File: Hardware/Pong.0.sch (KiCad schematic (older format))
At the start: 42 parts, among them IC1 ATMEGA644P-A, J1 DC, J2 USBMICRO-B, P1 ISP, SW1 SPST, X1 20 MHz

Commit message: Fleshed out main project, corrected errors, updated Project Log
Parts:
- removed BT1: 7.2VDC, symbol BATTERY
- removed C1, C10, C11, C2, C6, C7, C8: .1uF, symbol CSMALL
- removed C3, C9: 10uF, symbol CSMALL
- removed C4, C5: 8pF, symbol CSMALL
- removed IC1: ATMEGA644P-A, TQFP44, symbol ATMEGA644P-A
- removed J1: DC, symbol CONN_2
- removed J2: USBMICRO-B, symbol USBMICRO-B
- removed L1: 33uH, symbol INDUCTOR
- removed P1: ISP, symbol CONN_3X2
- removed R1, R2: 10k, symbol R
- removed R10, R11, R12, R13, R14, R15, R16, R17, R18, R19, R20, R21, R22, R3, R4, R5, R6, R7, R8, R9: 10K, symbol R
- removed S1: TL3315NF160Q, symbol TL3315NF160Q
- removed SW1: SPST, symbol SPST
- removed X1: 20 MHz, symbol CRYSTAL
- added BT?: BATTERY, symbol BATTERY
- added C? (x7): .1uF, symbol CSMALL
- added C? (x2): 8pF, symbol CSMALL
- added C? (x2): 10uF, symbol CSMALL
- added IC?: ATMEGA644P-A, TQFP44, symbol ATMEGA644P-A
- added L?: 33uH, symbol INDUCTOR
- added P?: CONN_2, symbol CONN_2
- added P?: ISP, symbol CONN_3X2
- added R?: R, symbol R
- added S?: TL3315NF160Q, symbol TL3315NF160Q
- added U?: USBMICRO-B, symbol USBMICRO-B
- added U?: SPX29150T-L-5-0/TR, symbol SPX29150T-L-5-0/TR
- added X?: 20MHz, symbol CRYSTAL
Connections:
- net labels added: X4, X5, X6, YA0, YA1, YA2, YB0, YB1, YB2
- net labels removed: +5V, SPX29150T-L-5-0/TR, SlaveSelect, UU00, UU01, UU02, UU03, UU04, UU05, UU06, UU07, UU08, UU09, UU10, UU11, UU12, UU13, UU14, UU15, UU16, UU17, UU18, UU19, Y0A, Y0B
- wire segments 158 -> 91

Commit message: Updated BOM and Requirements Document
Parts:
- removed BT?: BATTERY, symbol BATTERY
- removed C? (x7): .1uF, symbol CSMALL
- removed C? (x2): 8pF, symbol CSMALL
- removed C? (x2): 10uF, symbol CSMALL
- removed IC?: ATMEGA644P-A, TQFP44, symbol ATMEGA644P-A
- removed L?: 33uH, symbol INDUCTOR
- removed P?: CONN_2, symbol CONN_2
- removed P?: ISP, symbol CONN_3X2
- removed R?: R, symbol R
- removed S?: TL3315NF160Q, symbol TL3315NF160Q
- removed U?: USBMICRO-B, symbol USBMICRO-B
- removed U?: SPX29150T-L-5-0/TR, symbol SPX29150T-L-5-0/TR
- removed X?: 20MHz, symbol CRYSTAL
- added IC?: ATXMEGA64A4U-A, TQFP44, symbol ATXMEGA64A4U-A
- added U?: TPS61240, symbol TPS61240
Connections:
- net labels removed: AIN0, GND, MISO, MOSI, RESET, SCK, SMP, VCC, X0, X1, X2, X3, X4, X5, X6, YA0, YA1, YA2, YB0, YB1, YB2
- wire segments 91 -> 0
- no-connect marks 3 -> 0
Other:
- note added: "5V 0.45A\nBoost\nRegulator"
- note removed: "+"
- note removed: "-"

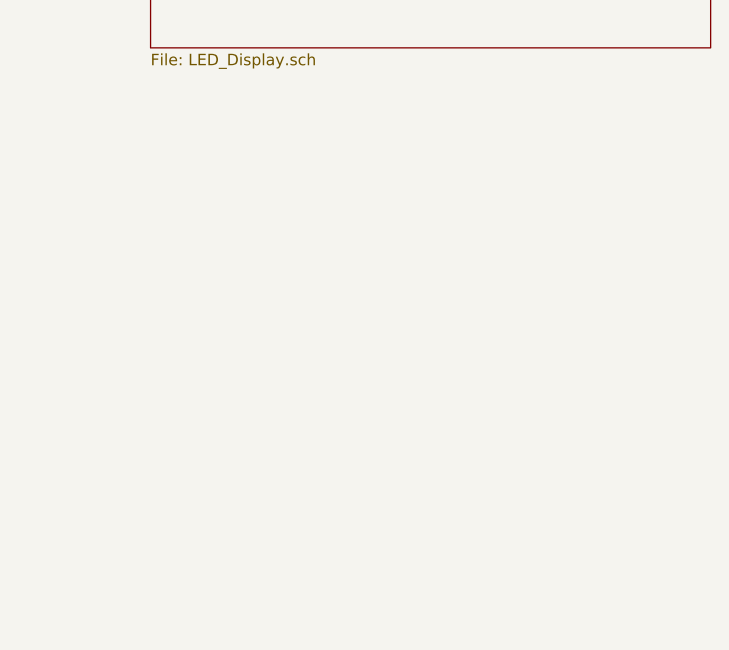
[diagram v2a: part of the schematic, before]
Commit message: Updated BOM and Schematic with significant components
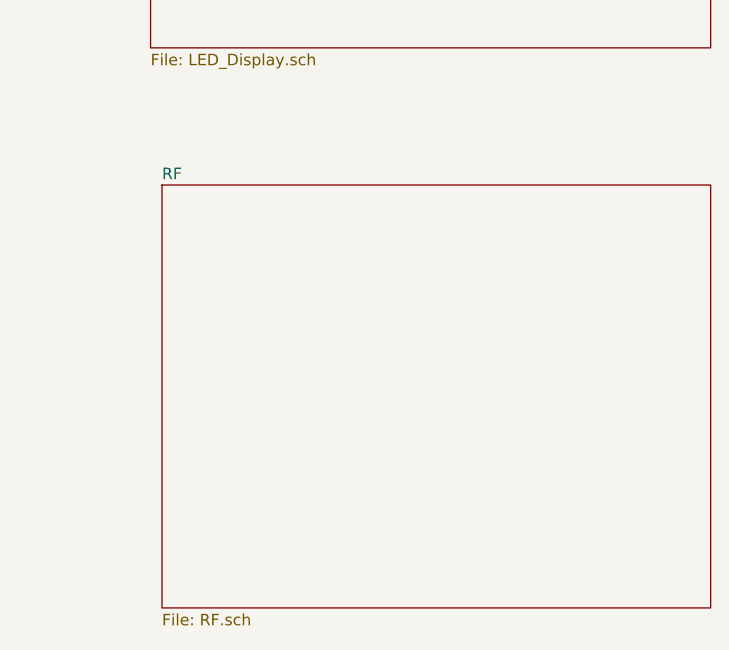
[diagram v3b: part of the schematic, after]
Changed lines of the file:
@@
 $Descr B 17000 11000
 encoding utf-8
-Sheet 1 2
+Sheet 1 3
 Title "Pong.0"
 Date "6 sep 2013"
@@
 6E 56 52 49 51 4E 59 71 7E 65 C5 4D 0F AF 00 BF F6 21 9D BA 45 88 9C 00 16 00 C0 66 90 E0 00 00
 AC 42 3B 38 00 00 AB 90 E0 00 00 AC 42 82 03 00 B0 EA FF 00 E3 76 B5 A7 81 B6 BC 08 00 00 00 00
-49 45 4E 44 AE 42 60 82 36 $EndBitmap
+49 45 4E 44 AE 42 60 82 7D $EndBitmap
 EndData
 $EndBitmap
@@
 Text Notes 6100 2100 0    60   ~ 0
 5V 0.45A\nBoost\nRegulator
+$Sheet
+S 13650 5150 2400 1850
+U 522A0B3B
+F0 "RF" 50
+F1 "RF.sch" 50
+$EndSheet
 $EndSCHEMATC

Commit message: Updated Schematic with Battery Manager and updated some uC pins
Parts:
- removed U?: TPS61240, symbol TPS61240
- added C? (x4): 0.1uF, ~, symbol CSMALL
- added C? (x2): 10uF, ~, symbol CSMALL
- added L?: 10uH, ~, symbol INDUCTOR
- added L?: BEAD, ~, symbol INDUCTOR
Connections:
- net labels added: 3_3V, GND, SCL, SDA, X0, X1, X2, X3, X4, X5, X6, X7, Y0A, Y0B, Y1A, Y1B, Y2A, Y2B, Y3A, Y3B
- wire segments 0 -> 45
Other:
- note removed: "5V 0.45A\nBoost\nRegulator"

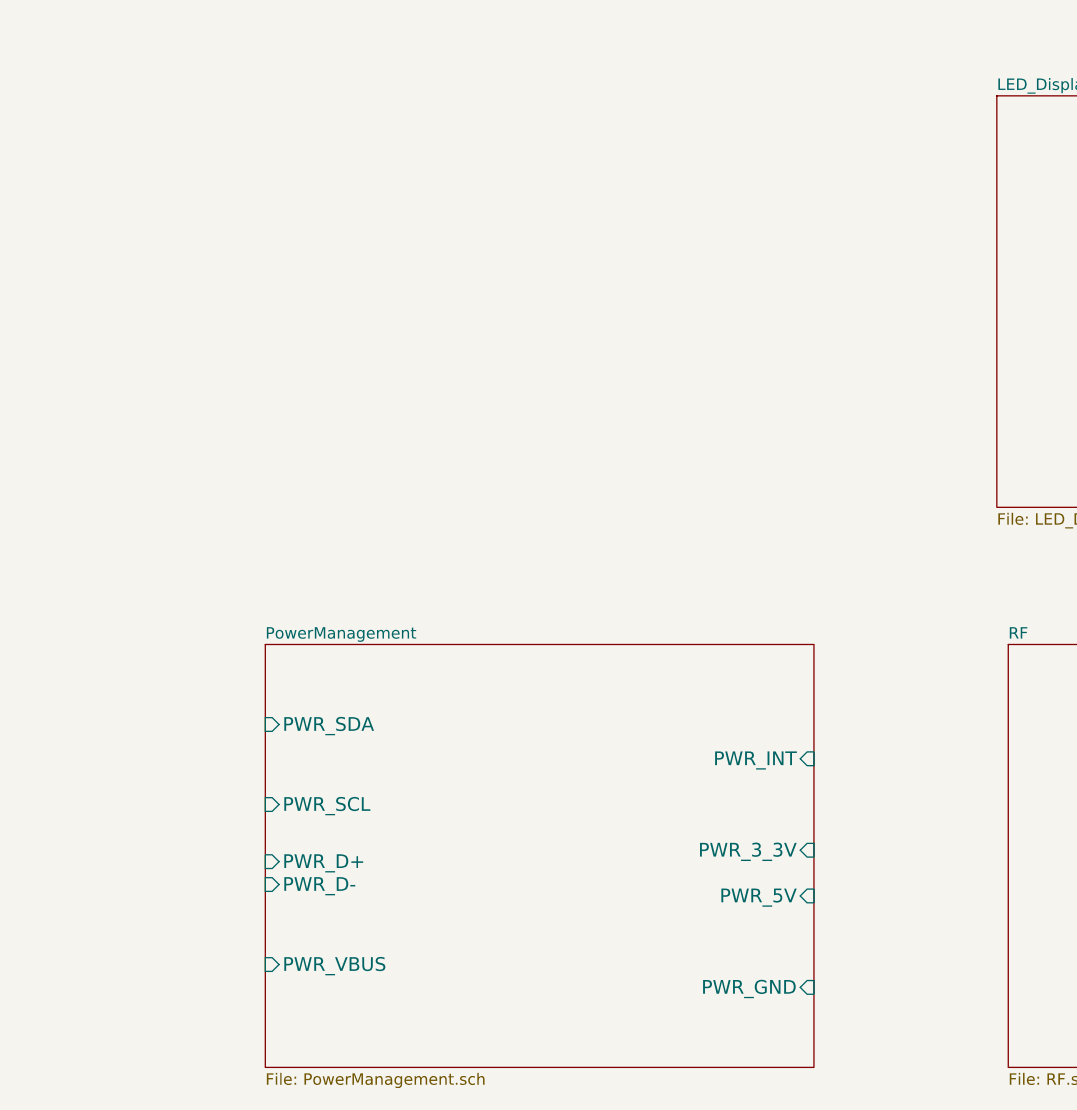
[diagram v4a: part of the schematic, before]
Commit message: Added sheet for QMatrix Sensors and Sliders
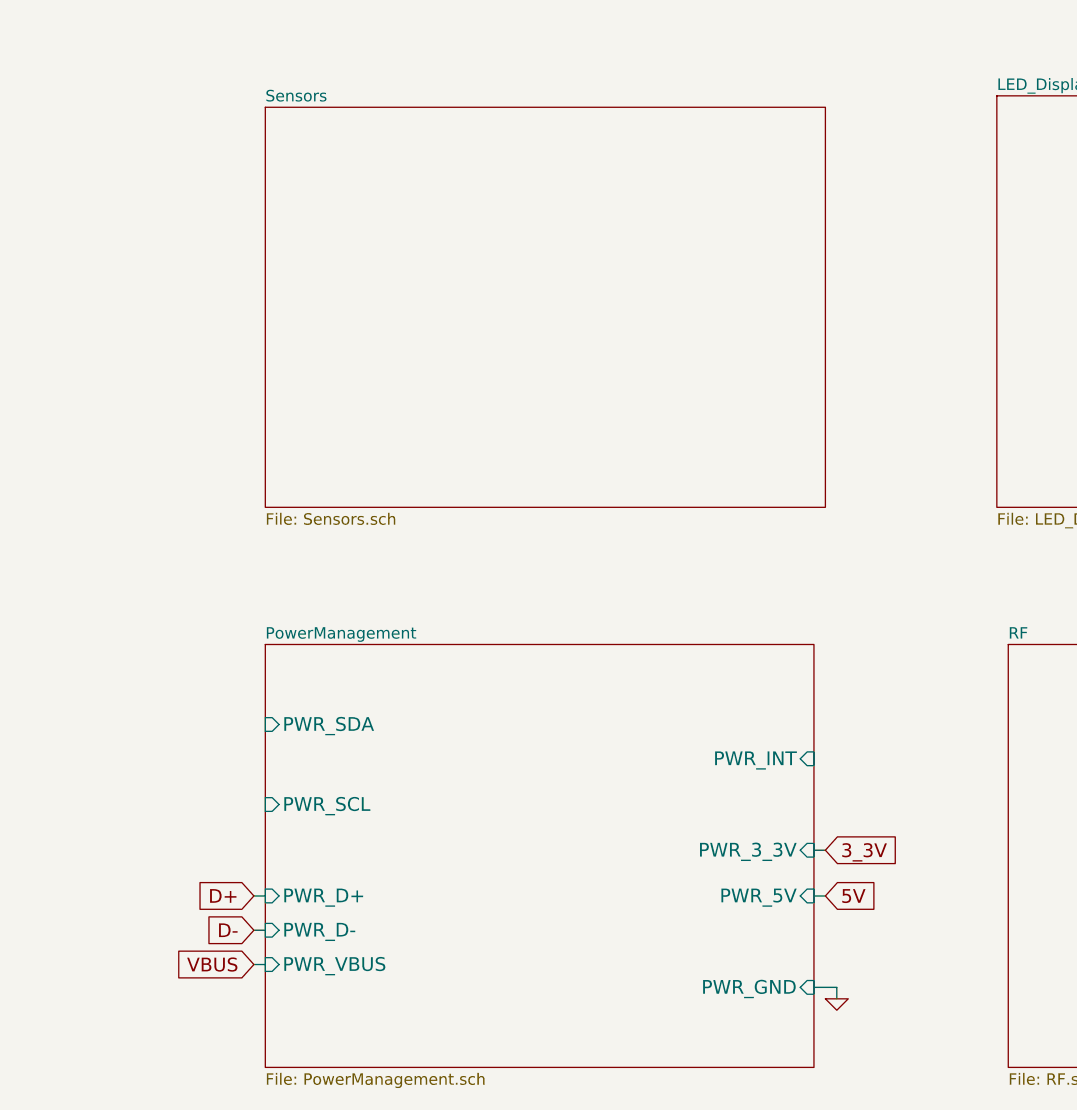
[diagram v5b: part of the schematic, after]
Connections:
- net labels added: 5V, D+, D-, VBUS
- wire segments 45 -> 52
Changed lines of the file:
@@
 6E 56 52 49 51 4E 59 71 7E 65 C5 4D 0F AF 00 BF F6 21 9D BA 45 88 9C 00 16 00 C0 66 90 E0 00 00
 AC 42 3B 38 00 00 AB 90 E0 00 00 AC 42 82 03 00 B0 EA FF 00 E3 76 B5 A7 81 B6 BC 08 00 00 00 00
-49 45 4E 44 AE 42 60 82 B6 $EndBitmap
+49 45 4E 44 AE 42 60 82 CE $EndBitmap
 EndData
 $EndBitmap
@@
 F2 "PWR_SDA" I L 10400 5500 60
 F3 "PWR_SCL" I L 10400 5850 60
-F4 "PWR_D-" I L 10400 6200 60
+F4 "PWR_D-" I L 10400 6400 60
 F5 "PWR_VBUS" I L 10400 6550 60
-F6 "PWR_D+" I L 10400 6100 60
+F6 "PWR_D+" I L 10400 6250 60
 F7 "PWR_INT" I R 12800 5650 60
 F8 "PWR_3_3V" I R 12800 6050 60
@@
 Connection ~ 5400 2850
 Connection ~ 4700 2850
+Wire Wire Line
+	12800 6050 12850 6050
+Wire Wire Line
+	12800 6250 12850 6250
+Text GLabel 12850 6050 2    60   Input ~ 0
+3_3V
+Text GLabel 12850 6250 2    60   Input ~ 0
+5V
+$Comp
+L GND #PWR?
+U 1 1 522CC6B0
+P 12900 6700
+F 0 "#PWR?" H 12900 6700 30  0001 C CNN
+F 1 "GND" H 12900 6630 30  0001 C CNN
+F 2 "" H 12900 6700 60  0000 C CNN
+F 3 "" H 12900 6700 60  0000 C CNN
+	1    12900 6700
+	1    0    0    -1
+$EndComp
+Wire Wire Line
+	12800 6650 12900 6650
+Wire Wire Line
+	12900 6650 12900 6700
+Wire Wire Line
+	10400 6250 10350 6250
+Wire Wire Line
+	10400 6400 10350 6400
+Wire Wire Line
+	10400 6550 10350 6550
+Text GLabel 10350 6250 0    60   Input ~ 0
+D+
+Text GLabel 10350 6400 0    60   Input ~ 0
+D-
+Text GLabel 10350 6550 0    60   Input ~ 0
+VBUS
+$Sheet
+S 10400 2800 2450 1750
+U 522CCF9A
+F0 "Sensors" 50
+F1 "Sensors.sch" 50
+$EndSheet
 $EndSCHEMATC

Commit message: Added logos, continued updating schematics.
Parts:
- removed C? (x4): 0.1uF, ~, symbol CSMALL
- removed C? (x2): 10uF, ~, symbol CSMALL
- removed IC?: ATXMEGA64A4U-A, TQFP44, symbol ATXMEGA64A4U-A
- removed L?: 10uH, ~, symbol INDUCTOR
- removed L?: BEAD, ~, symbol INDUCTOR
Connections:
- net labels removed: SCL, SDA, X0, X1, X2, X3, X4, X5, X6, X7, Y0A, Y0B, Y1A, Y1B, Y2A, Y2B, Y3A, Y3B
- wire segments 52 -> 7

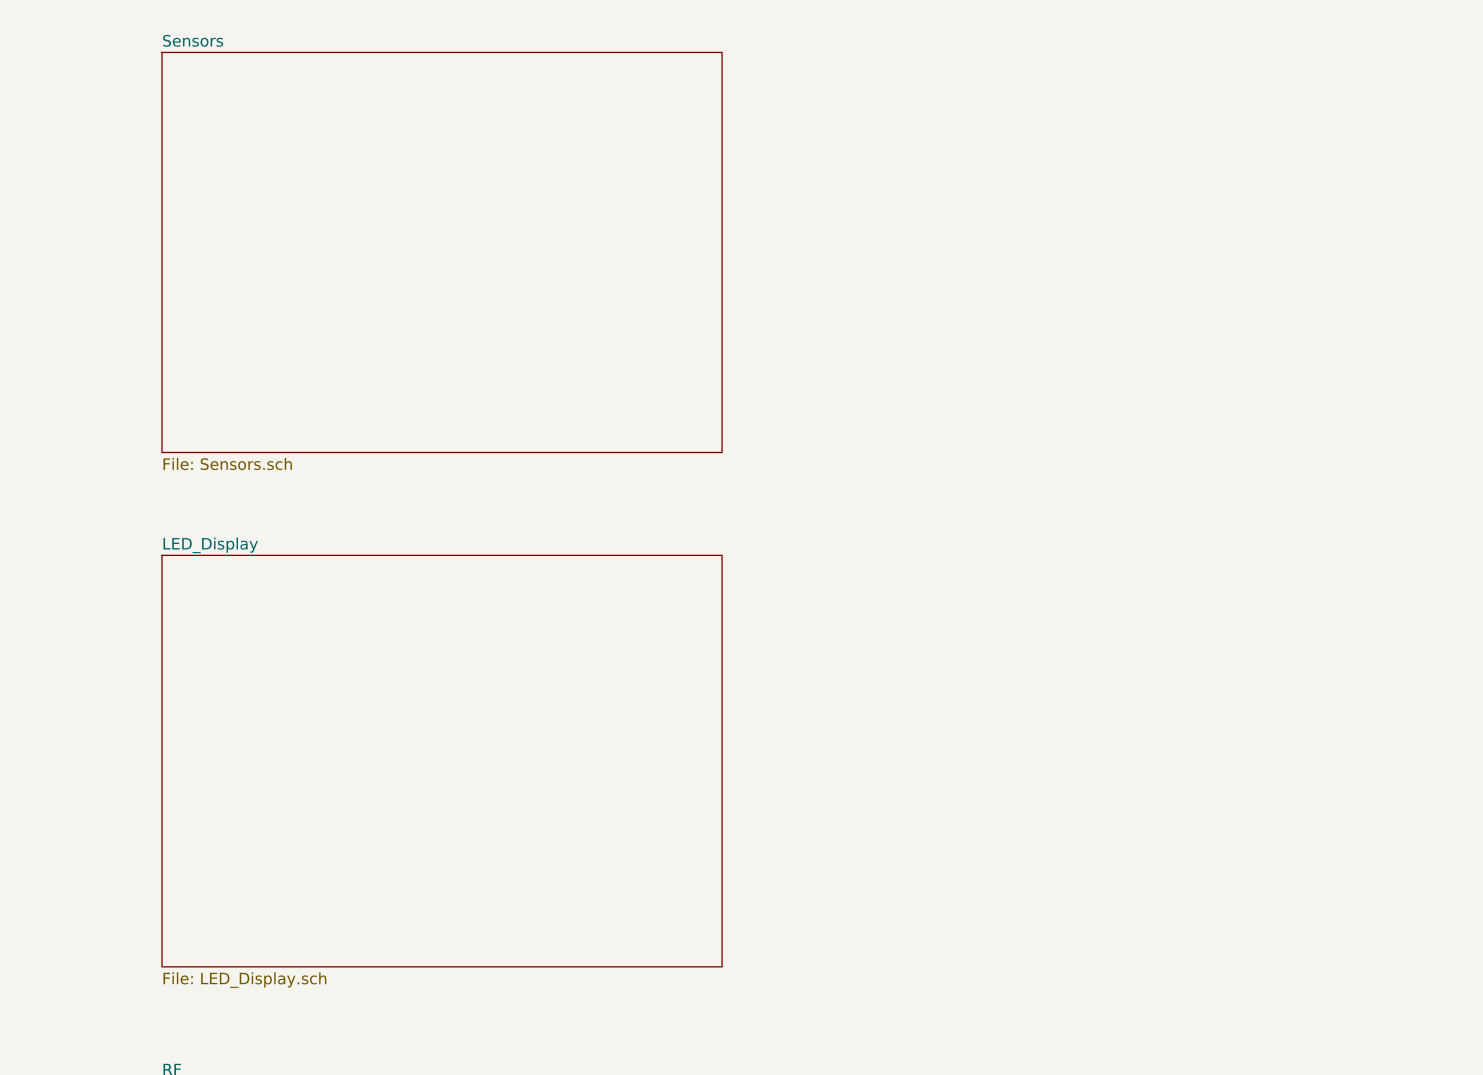
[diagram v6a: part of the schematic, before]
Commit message: Added Slider. Imported Sheet Pins. Made other minor adjustments to schematics.
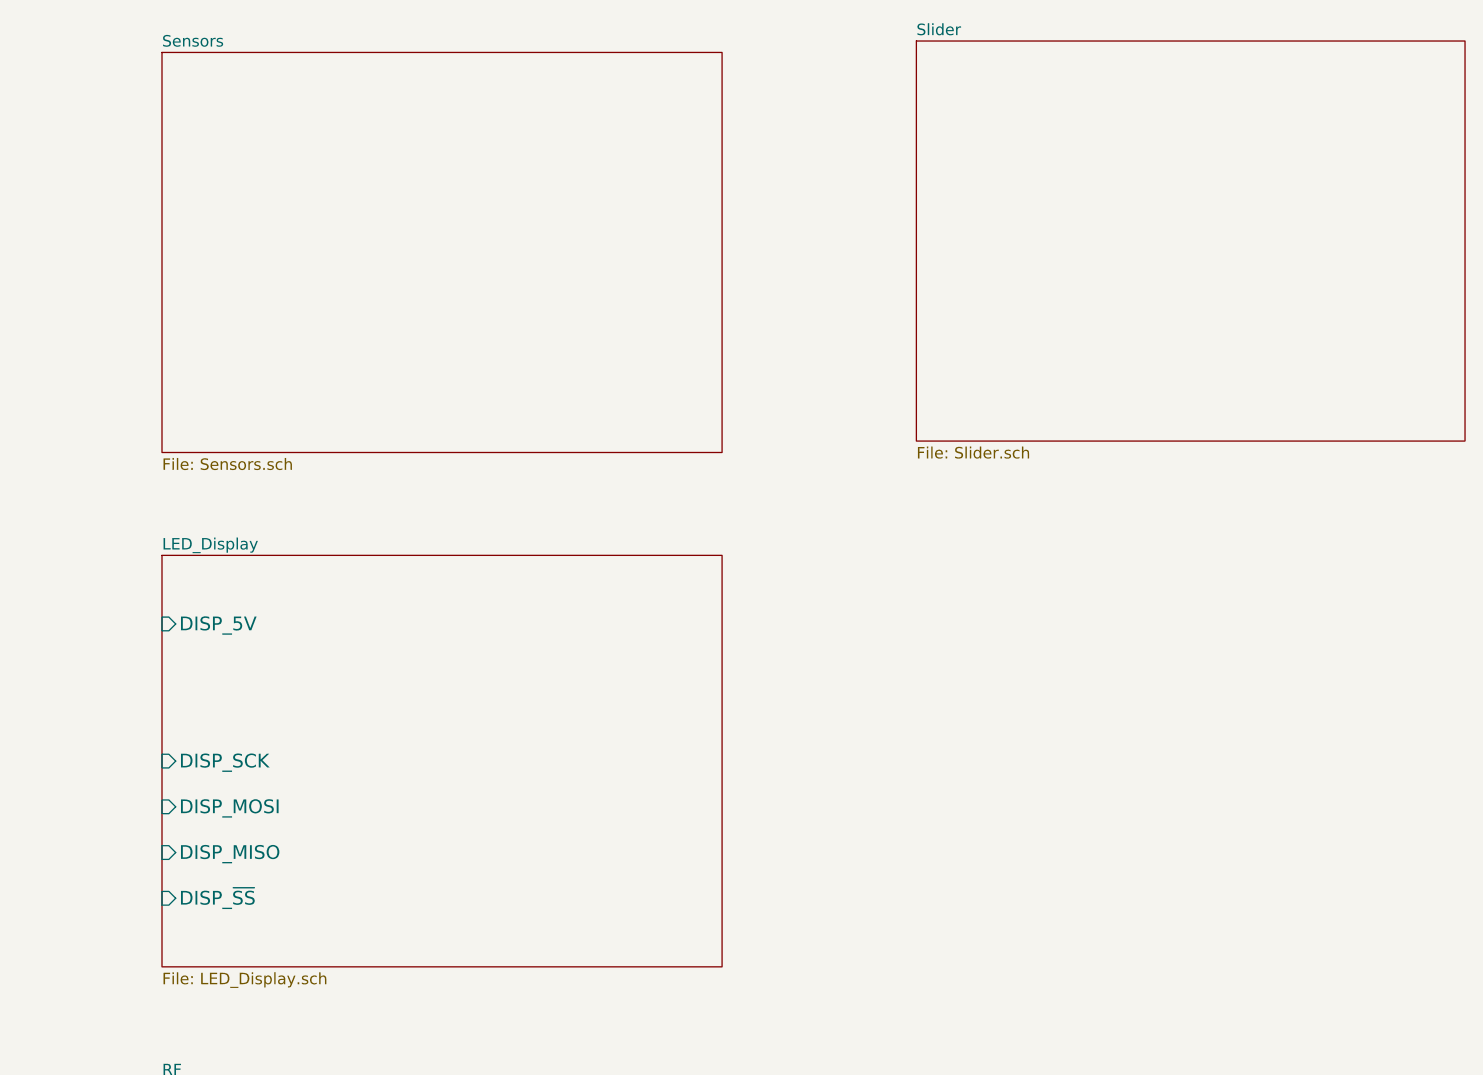
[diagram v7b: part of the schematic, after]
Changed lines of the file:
@@
 $Descr B 17000 11000
 encoding utf-8
-Sheet 1 6
+Sheet 1 7
 Title "Pong.0"
-Date "9 sep 2013"
+Date "12 sep 2013"
 Rev "0.2"
 Comp "Projects and Stuff LLC"
@@
 6E 56 52 49 51 4E 59 71 7E 65 C5 4D 0F AF 00 BF F6 21 9D BA 45 88 9C 00 16 00 C0 66 90 E0 00 00
 AC 42 3B 38 00 00 AB 90 E0 00 00 AC 42 82 03 00 B0 EA FF 00 E3 76 B5 A7 81 B6 BC 08 00 00 00 00
-49 45 4E 44 AE 42 60 82 E5 $EndBitmap
+49 45 4E 44 AE 42 60 82 DC $EndBitmap
 EndData
 $EndBitmap
@@
 F0 "LED_Display" 50
 F1 "LED_Display.sch" 50
+F2 "DISP_SCK" I L 8450 4450 60
+F3 "DISP_MOSI" I L 8450 4650 60
+F4 "DISP_MISO" I L 8450 4850 60
+F5 "DISP_~SS" I L 8450 5050 60
+F6 "DISP_5V" I L 8450 3850 60
 $EndSheet
 $Sheet
@@
 EndData
 $EndBitmap
+$Sheet
+S 11750 1300 2400 1750
+U 5231F823
+F0 "Slider" 50
+F1 "Slider.sch" 50
+$EndSheet
 $EndSCHEMATC
